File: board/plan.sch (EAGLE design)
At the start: 14 parts, among them IC1 TINY24/44/84-SSU, X1 250-404, X2 250-408

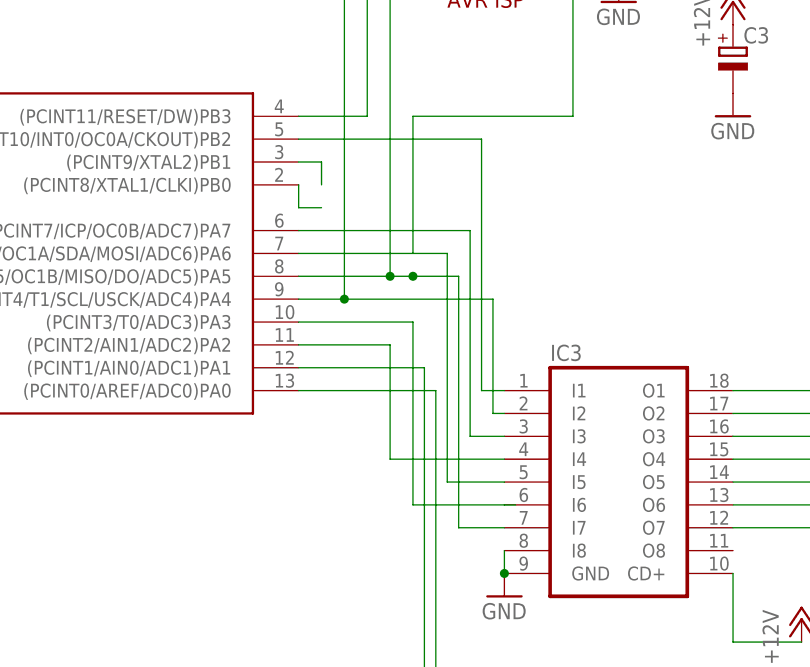
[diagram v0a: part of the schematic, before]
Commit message: Fixed missing connection to ADC input
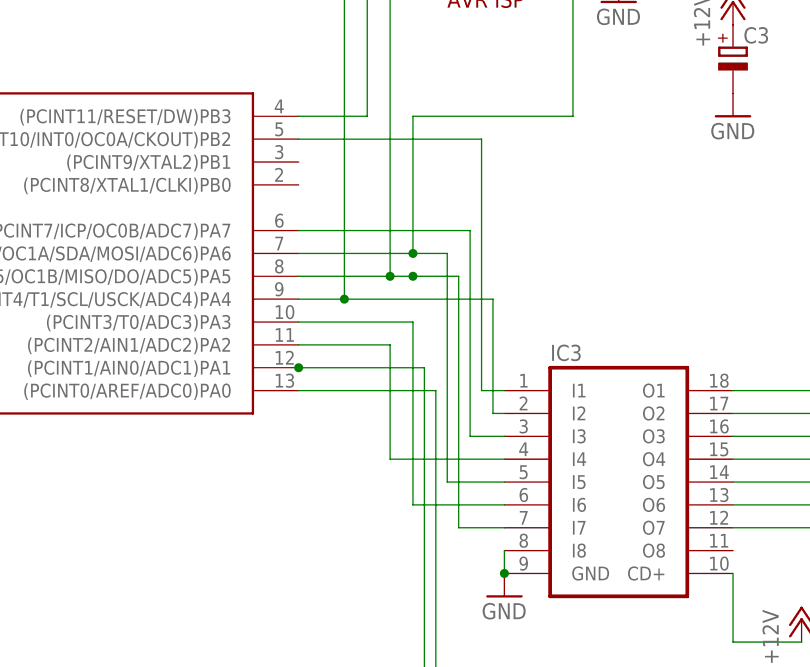
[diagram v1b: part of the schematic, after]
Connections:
- removed net N$21: IC1.(PCINT8/XTAL1/CLKI)PB0
- removed net N$9: IC1.(PCINT9/XTAL2)PB1
- net N$18: now also IC1.(PCINT1/AIN0/ADC1)PA1
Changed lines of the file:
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@@
 <setting verticaltext="up"/>
 </settings>
-<grid distance="0.05" unitdist="inch" unit="inch" style="lines" multiple="1" display="no" altdistance="0.01" altunitdist="inch" altunit="inch"/>
+<grid distance="0.1" unitdist="inch" unit="inch" style="lines" multiple="1" display="no" altdistance="0.01" altunitdist="inch" altunit="inch"/>
 <layers>
 <layer number="1" name="Top" color="4" fill="1" visible="no" active="no"/>
@@
 <pinref part="IC3" gate="G$1" pin="I5"/>
 <wire x1="90.17" y1="53.34" x2="96.52" y2="53.34" width="0.1524" layer="91"/>
+<junction x="86.36" y="78.74"/>
 </segment>
 </net>
@@
 <wire x1="85.09" y1="2.54" x2="85.09" y2="1.27" width="0.1524" layer="91"/>
 <junction x="85.09" y="2.54"/>
+<pinref part="IC1" gate="1" pin="(PCINT1/AIN0/ADC1)PA1"/>
+<junction x="73.66" y="66.04"/>
 </segment>
 </net>
@@
 <wire x1="86.36" y1="71.12" x2="86.36" y2="50.8" width="0.1524" layer="91"/>
 <pinref part="IC3" gate="G$1" pin="I6"/>
-<wire x1="96.52" y1="50.8" x2="97.79" y2="50.8" width="0.1524" layer="91"/>
 <wire x1="86.36" y1="50.8" x2="96.52" y2="50.8" width="0.1524" layer="91"/>
 </segment>
@@
 </segment>
 </net>
-<net name="N$9" class="0">
-<segment>
-<pinref part="IC1" gate="1" pin="(PCINT9/XTAL2)PB1"/>
-<wire x1="73.66" y1="88.9" x2="76.2" y2="88.9" width="0.1524" layer="91"/>
-<wire x1="76.2" y1="88.9" x2="76.2" y2="86.36" width="0.1524" layer="91"/>
-</segment>
-</net>
-<net name="N$21" class="0">
-<segment>
-<pinref part="IC1" gate="1" pin="(PCINT8/XTAL1/CLKI)PB0"/>
-<wire x1="73.66" y1="86.36" x2="73.66" y2="83.82" width="0.1524" layer="91"/>
-<wire x1="73.66" y1="83.82" x2="76.2" y2="83.82" width="0.1524" layer="91"/>
-</segment>
-</net>
